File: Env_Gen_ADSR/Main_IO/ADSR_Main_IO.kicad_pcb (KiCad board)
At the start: 2 copper layers, 30 x 111.8 mm, 27 parts, among them J1 Gate, J2 Trigger, J3 Env, J4 Conn_01x16, U1 AS3310, U2 TL071

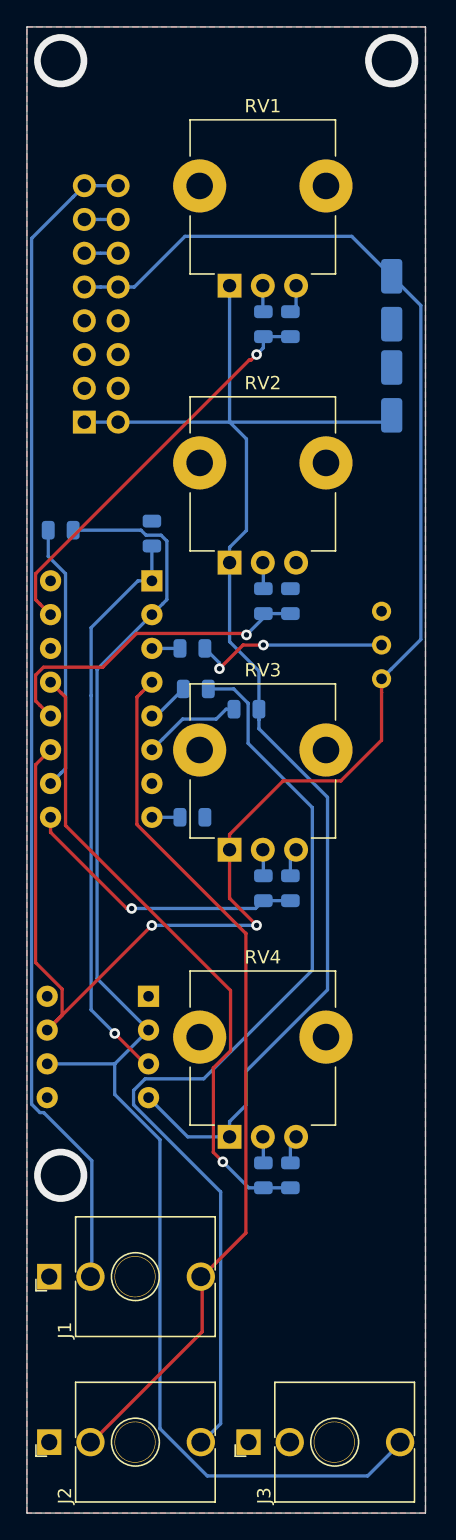
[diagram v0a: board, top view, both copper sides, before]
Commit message: Fix envelope generator front panel size and alignment with IO board.
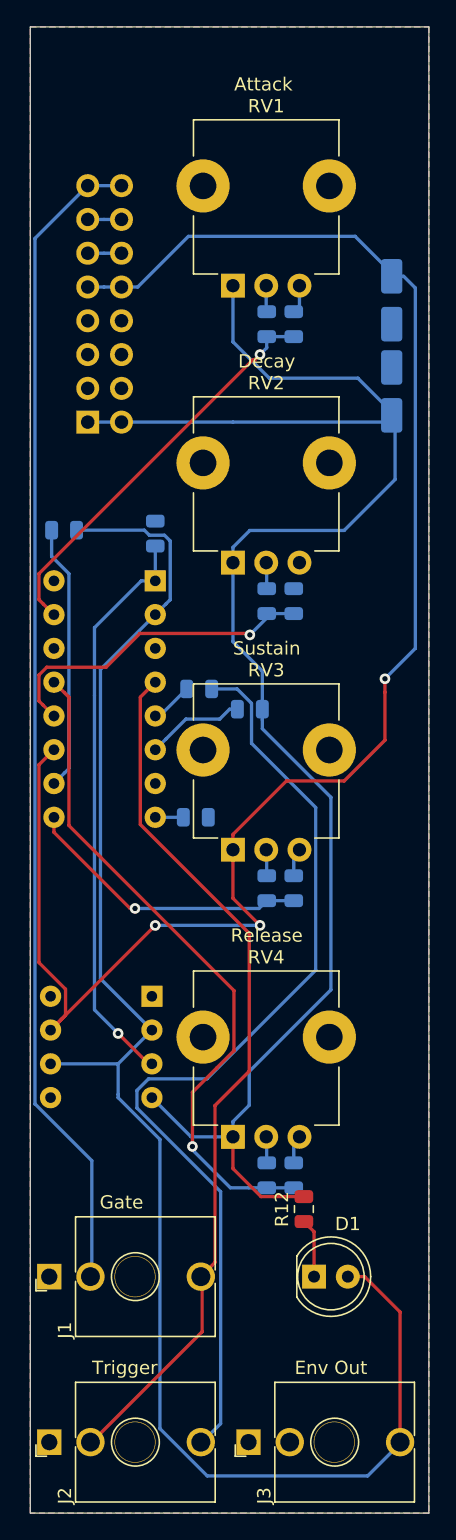
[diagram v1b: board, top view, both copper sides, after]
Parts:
- removed R10: 10K, Resistor_SMD:R_0805_2012Metric
- removed RV5: 100K, Potentiometer_THT:Potentiometer_Bourns_3296W_Vertical
- added D1: LED, Eurorack:LED_D5.0mm, F.Cu at (86.4, 142.2)
- added R12: R_US, Resistor_SMD:R_0805_2012Metric, F.Cu at (84.3, 137.2)
- moved C2 0.25 mm to (76.2, 107.7)
- moved C3 0.25 mm to (73.2, 86.4)
- moved J4 0.25 mm to (68.1, 78.0)
- moved R1 0.25 mm to (81.5, 70.6)
- moved R2 0.25 mm to (83.6, 70.6)
- moved R3 0.25 mm to (81.5, 91.4)
- moved R4 0.25 mm to (83.6, 91.4)
- moved R5 0.25 mm to (81.5, 113.0)
- moved R6 0.25 mm to (83.6, 113.0)
- moved R7 0.25 mm to (81.5, 134.6)
- moved R8 0.25 mm to (83.6, 134.6)
- moved RV1 0.25 mm to (81.5, 60.2)
- moved RV2 0.25 mm to (81.5, 81.0)
- moved RV3 0.25 mm to (81.5, 102.6)
- moved RV4 0.25 mm to (81.5, 124.2)
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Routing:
- net -12V: track 101.8 -> 128.1 mm
- net Net-(R10-Pad2): track 14.9 -> 0.00 mm, vias 2 -> 0
- net Net-(D1-Pad2): track 106.6 -> 121.3 mm
- net Net-(D1-Pad1): track 0.00 -> 4.46 mm
- net /Release: track 48.4 -> 50.7 mm
- net Net-(U1-Pad3): track 2.11 -> 0.00 mm
- net +12V: track 126.8 -> 126.9 mm, vias 2 -> 3
- net GNDREF: vias 3 -> 0
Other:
- board text added: "Attack"
- board text added: "Decay"
- board text added: "Env Out"
- board text added: "Gate"
- board text added: "Release"
- board text added: "Sustain"
- board text added: "Trigger"

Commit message: Clean up envelope generator boards
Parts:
- added REF**: OSHW-Logo2_7.3x6mm_SilkScreen, Symbol:OSHW-Logo2_7.3x6mm_SilkScreen, B.Cu at (87.6, 54.1)
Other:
- board text added: "ADSR Env Gen Main Board Rev 2"
- board text added: "WH"

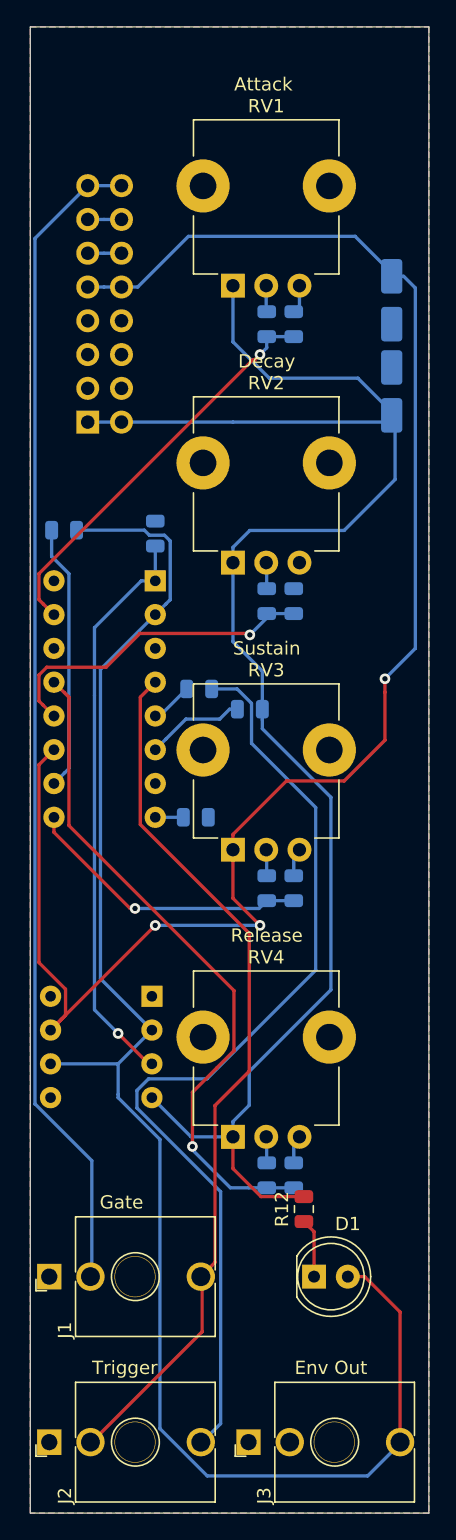
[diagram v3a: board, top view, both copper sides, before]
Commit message: Clean up envelope gen board
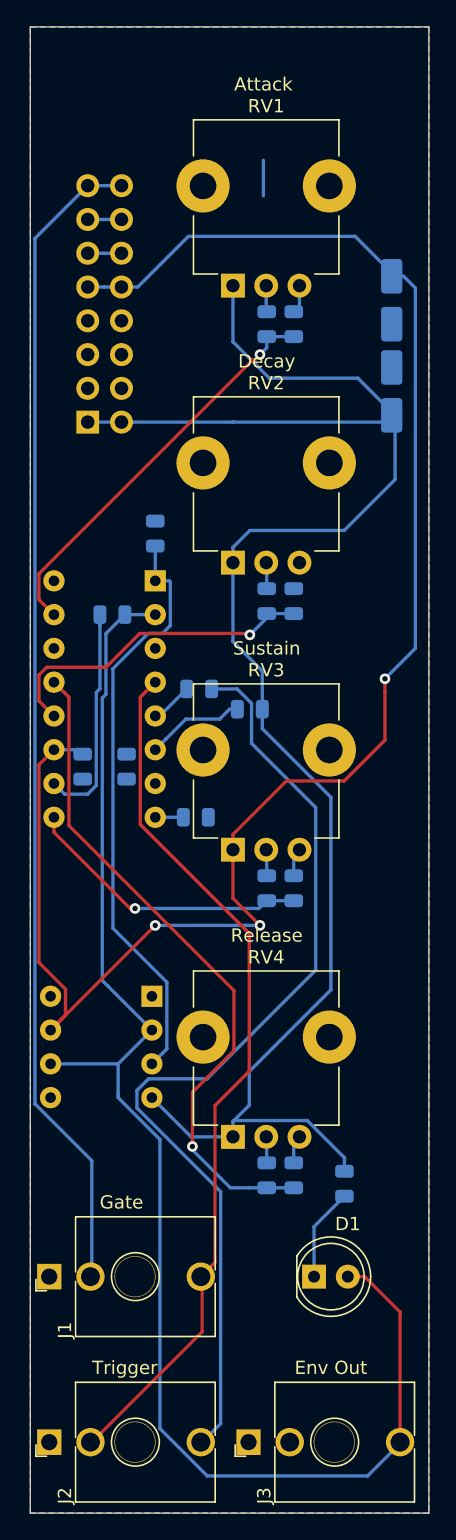
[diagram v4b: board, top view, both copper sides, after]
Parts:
- removed REF**: OSHW-Logo2_7.3x6mm_SilkScreen, Symbol:OSHW-Logo2_7.3x6mm_SilkScreen
- added C6: 0.1uF, Capacitor_SMD:C_0805_2012Metric, B.Cu at (71.0, 103.9)
- added C7: 0.1uF, Capacitor_SMD:C_0805_2012Metric, B.Cu at (67.7, 103.9)
- R12: moved to B.Cu
- moved R9 7.32 mm to (69.9, 92.5)
- moved R12 3.59 mm to (87.4, 135.3)
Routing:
- net Net-(D1-Pad2): track 121.3 -> 108.7 mm
- net +12V: track 126.9 -> 129.7 mm
- net (no net): track 0.00 -> 2.67 mm
- net Net-(D1-Pad1): track 4.46 -> 6.99 mm
- net Net-(R9-Pad1): track 20.1 -> 17.5 mm
- net -12V: track 128.1 -> 130.1 mm
- net Net-(C3-Pad1): track 43.4 -> 44.8 mm, vias 1 -> 0

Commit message: Fix backwards knobs
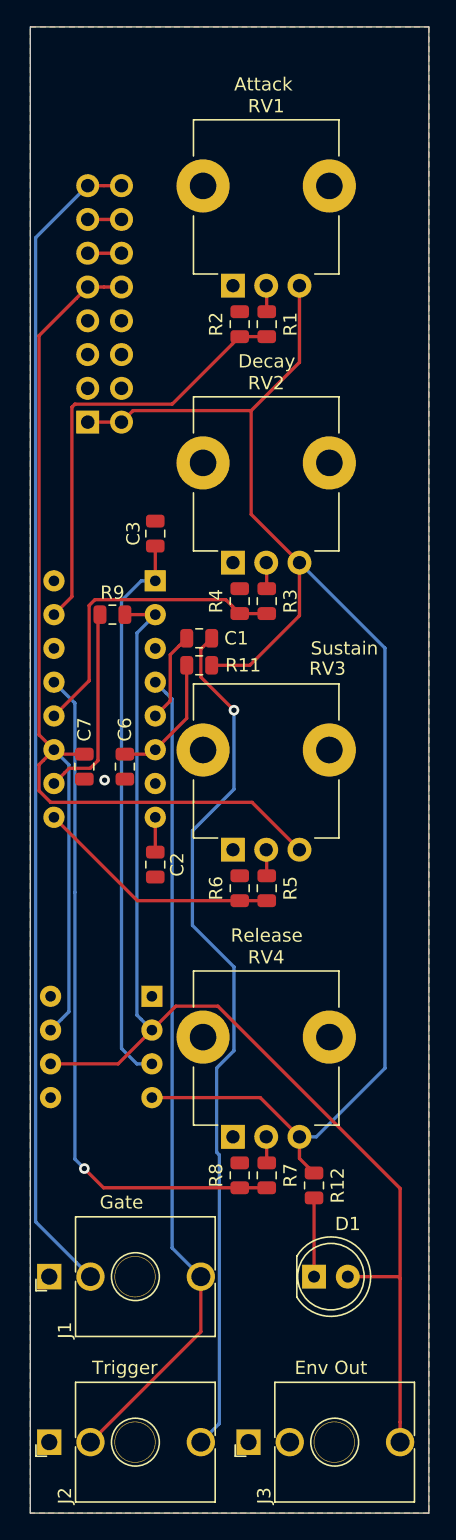
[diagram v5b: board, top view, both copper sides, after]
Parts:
- removed C4, C5: CP1, Capacitor_SMD:CP_Elec_4x3
- C1, C2, C3, C6, C7, R1, R11, R12, R2, R3, R4, R7, R8, R9: moved to F.Cu
- R5: value R_US -> 22K; moved to F.Cu
- R6: value R_US -> 450; moved to F.Cu
- moved R11 5.04 mm to (76.5, 96.3)
- moved C2 4.68 mm to (73.2, 111.3), turned to 270 degrees
- moved R2 4.06 mm to (79.5, 70.6)
- moved R4 4.06 mm to (79.5, 91.4)
- moved R6 4.06 mm to (79.5, 113.0)
- moved R8 4.06 mm to (79.5, 134.6)
- moved C1 3.81 mm to (76.5, 94.2)
- moved R12 2.29 mm to (85.1, 135.4)
- moved C6 0.13 mm to (70.9, 103.9)
- moved C7 0.13 mm to (67.8, 103.9)
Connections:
- RV1 pad 1: -12V -> GNDREF
- RV1 pad 3: GNDREF -> -12V
- RV2 pad 1: -12V -> GNDREF
- RV2 pad 3: GNDREF -> -12V
- RV3 pad 1: +12V -> GNDREF
- RV3 pad 3: GNDREF -> +12V
- RV4 pad 1: -12V -> GNDREF
- RV4 pad 3: GNDREF -> -12V
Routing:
- net +12V: track 129.7 -> 88.8 mm, vias 3 -> 0
- net Net-(D1-Pad2): track 108.7 -> 91.4 mm
- net -12V: track 130.1 -> 113.4 mm
- net /Trigger: track 72.3 -> 65.6 mm, vias 0 -> 1
- net GNDREF: track 6.40 -> 0.00 mm, vias 0 -> 1
- net /Gate: track 66.0 -> 62.0 mm
- net Net-(C1-Pad1): track 3.21 -> 6.82 mm
- net /Sustain: track 21.8 -> 18.6 mm, vias 1 -> 0
- net (no net): track 2.67 -> 0.00 mm
- net Net-(C3-Pad1): track 44.8 -> 42.2 mm
- net Net-(R9-Pad1): track 17.5 -> 15.1 mm
- net /Attack: track 30.6 -> 33.0 mm, vias 1 -> 0
- net Net-(C6-Pad1): track 7.91 -> 9.75 mm
- net /Decay: track 24.9 -> 23.4 mm, vias 1 -> 0
- net /Release: track 50.7 -> 51.8 mm
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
